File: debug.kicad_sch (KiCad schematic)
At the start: 18 parts, among them J9 USB_C_Receptacle_USB2.0, Q28 MMBT3904, Q29 MMBT3904, U16 CH340G, Y1 12MHz

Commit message: Partial layout
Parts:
- added U18: SRV05-4, Package_TO_SOT_SMD:SOT-23-6, symbol Power_Protection:SRV05-4
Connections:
- net GND: now also U18.5 (VP)
- net VBUS: now also U18.2 (VN)
- net at J9.A6 (D+), J9.B6 (D+), U16.5 (UD+): now also U18.1 (IO1)
- net at J9.A7 (D-), J9.B7 (D-), U16.6 (UD-): now also U18.3 (IO2)
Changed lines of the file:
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@@
 (kicad_sch (version 20211123) (generator eeschema)
   (paper "A4")
+  (junction (at 92.71 88.9) (diameter 0) (color 0 0 0 0)
+  )
   (junction (at 78.74 81.28) (diameter 0) (color 0 0 0 0)
   )
@@
   )
   (junction (at 124.46 72.39) (diameter 0) (color 0 0 0 0)
+  )
+  (junction (at 91.44 91.44) (diameter 0) (color 0 0 0 0)
   )
   (junction (at 41.91 113.03) (diameter 0) (color 0 0 0 0)
@@
     (stroke (width 0) (type default) (color 0 0 0 0))
   )
+  (wire (pts (xy 91.44 91.44) (xy 88.9 91.44))
+    (stroke (width 0) (type default) (color 0 0 0 0))
+  )
   (wire (pts (xy 123.19 68.58) (xy 123.19 72.39))
     (stroke (width 0) (type default) (color 0 0 0 0))
@@
     (stroke (width 0) (type default) (color 0 0 0 0))
   )
+  (wire (pts (xy 90.17 109.22) (xy 91.44 109.22))
+    (stroke (width 0) (type default) (color 0 0 0 0))
+  )
   (wire (pts (xy 31.75 113.03) (xy 41.91 113.03))
     (stroke (width 0) (type default) (color 0 0 0 0))
@@
     (stroke (width 0) (type default) (color 0 0 0 0))
   )
+  (wire (pts (xy 92.71 88.9) (xy 87.63 88.9))
+    (stroke (width 0) (type default) (color 0 0 0 0))
+  )
   (wire (pts (xy 114.3 96.52) (xy 101.6 96.52))
     (stroke (width 0) (type default) (color 0 0 0 0))
@@
     (stroke (width 0) (type default) (color 0 0 0 0))
   )
+  (wire (pts (xy 90.17 114.3) (xy 92.71 114.3))
+    (stroke (width 0) (type default) (color 0 0 0 0))
+  )
   (wire (pts (xy 134.62 101.6) (xy 146.05 101.6))
     (stroke (width 0) (type default) (color 0 0 0 0))
@@
     (stroke (width 0) (type default) (color 0 0 0 0))
   )
-  (wire (pts (xy 114.3 88.9) (xy 87.63 88.9))
+  (wire (pts (xy 114.3 88.9) (xy 92.71 88.9))
     (stroke (width 0) (type default) (color 0 0 0 0))
   )
@@
     (stroke (width 0) (type default) (color 0 0 0 0))
   )
+  (wire (pts (xy 77.47 96.52) (xy 77.47 99.06))
+    (stroke (width 0) (type default) (color 0 0 0 0))
+  )
   (wire (pts (xy 87.63 88.9) (xy 87.63 91.44))
     (stroke (width 0) (type default) (color 0 0 0 0))
@@
     (stroke (width 0) (type default) (color 0 0 0 0))
   )
-  (wire (pts (xy 114.3 91.44) (xy 88.9 91.44))
+  (wire (pts (xy 114.3 91.44) (xy 91.44 91.44))
     (stroke (width 0) (type default) (color 0 0 0 0))
   )
@@
     (stroke (width 0) (type default) (color 0 0 0 0))
   )
+  (wire (pts (xy 77.47 124.46) (xy 77.47 125.73))
+    (stroke (width 0) (type default) (color 0 0 0 0))
+  )
   (wire (pts (xy 143.51 99.06) (xy 143.51 104.14))
     (stroke (width 0) (type default) (color 0 0 0 0))
@@
   )
   (wire (pts (xy 124.46 72.39) (xy 124.46 76.2))
+    (stroke (width 0) (type default) (color 0 0 0 0))
+  )
+  (wire (pts (xy 91.44 109.22) (xy 91.44 91.44))
+    (stroke (width 0) (type default) (color 0 0 0 0))
+  )
+  (wire (pts (xy 92.71 88.9) (xy 92.71 114.3))
     (stroke (width 0) (type default) (color 0 0 0 0))
   )
@@
       (effects (font (size 1.27 1.27)) hide)
     )
-    (property "Datasheet" "https://www.usb.org/sites/default/files/documents/usb_type-c.zip" (id 3) (at 53.34 88.9 0)
+    (property "Datasheet" "https://datasheet.lcsc.com/lcsc/2103051833_Jing-Extension-of-the-Electronic-Co.-918-418K2023S40001_C167321.pdf" (id 3) (at 53.34 88.9 0)
       (effects (font (size 1.27 1.27)) hide)
     )
@@
     (pin "2")
   )
+  (symbol (lib_id "Power_Protection:SRV05-4") (at 77.47 111.76 180) (unit 1)
+    (in_bom yes) (on_board yes) (fields_autoplaced)
+    (property "Reference" "U18" (id 0) (at 77.2413 97.9002 0)
+      (effects (font (size 1.27 1.27)) (justify right))
+    )
+    (property "Value" "SRV05-4" (id 1) (at 77.2413 100.4371 0)
+      (effects (font (size 1.27 1.27)) (justify right))
+    )
+    (property "Footprint" "Package_TO_SOT_SMD:SOT-23-6" (id 2) (at 59.69 100.33 0)
+      (effects (font (size 1.27 1.27)) hide)
+    )
+    (property "Datasheet" "http://www.onsemi.com/pub/Collateral/SRV05-4-D.PDF" (id 3) (at 77.47 111.76 0)
+      (effects (font (size 1.27 1.27)) hide)
+    )
+    (property "LCSC" "C85364" (id 4) (at 77.47 111.76 0)
+      (effects (font (size 1.27 1.27)) hide)
+    )
+    (pin "1")
+    (pin "2")
+    (pin "3")
+    (pin "4")
+    (pin "5")
+    (pin "6")
+  )
   (symbol (lib_id "Device:C_Small") (at 101.6 111.76 0) (mirror x) (unit 1)
     (in_bom yes) (on_board yes) (fields_autoplaced)
@@
     (pin "2")
   )
+  (symbol (lib_id "power:VBUS") (at 77.47 96.52 0) (unit 1)
+    (in_bom yes) (on_board yes) (fields_autoplaced)
+    (property "Reference" "#PWR0305" (id 0) (at 77.47 100.33 0)
+      (effects (font (size 1.27 1.27)) hide)
+    )
+    (property "Value" "VBUS" (id 1) (at 77.47 92.9442 0))
+    (property "Footprint" "" (id 2) (at 77.47 96.52 0)
+      (effects (font (size 1.27 1.27)) hide)
+    )
+    (property "Datasheet" "" (id 3) (at 77.47 96.52 0)
+      (effects (font (size 1.27 1.27)) hide)
+    )
+    (pin "1")
+  )
   (symbol (lib_id "Device:C_Small") (at 118.11 72.39 270) (mirror x) (unit 1)
     (in_bom yes) (on_board yes)
@@
       (effects (font (size 1.27 1.27)) hide)
     )
+    (pin "1")
+  )
+  (symbol (lib_id "power:GND") (at 77.47 125.73 0) (unit 1)
+    (in_bom yes) (on_board yes) (fields_autoplaced)
+    (property "Reference" "#PWR0306" (id 0) (at 77.47 132.08 0)
+      (effects (font (size 1.27 1.27)) hide)
+    )
+    (property "Value" "GND" (id 1) (at 77.47 130.1734 0))
+    (property "Footprint" "" (id 2) (at 77.47 125.73 0)
+      (effects (font (size 1.27 1.27)) hide)
+    )
+    (property "Datasheet" "" (id 3) (at 77.47 125.73 0)
+      (effects (font (size 1.27 1.27)) hide)
+    )

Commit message: Fix footprint origins for JLC assembly
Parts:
- U16: value CH340G -> CH340C; LCSC C14267 -> C84681
- Y1: value 12MHz -> 12MHz (DNP); now left out of the parts list
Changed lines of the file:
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@@
       (effects (font (size 1.27 1.27)) (justify left))
     )
-    (property "Value" "CH340G" (id 1) (at 126.4794 108.7073 0)
+    (property "Value" "CH340C" (id 1) (at 126.4794 108.7073 0)
       (effects (font (size 1.27 1.27)) (justify left))
     )
@@
       (effects (font (size 1.27 1.27)) hide)
     )
-    (property "LCSC" "C14267" (id 4) (at 124.46 91.44 0)
+    (property "LCSC" "C84681" (id 4) (at 124.46 91.44 0)
       (effects (font (size 1.27 1.27)) hide)
     )
@@
   )
   (symbol (lib_id "Device:Crystal_GND24_Small") (at 105.41 107.95 0) (unit 1)
-    (in_bom yes) (on_board yes)
+    (in_bom no) (on_board yes)
     (property "Reference" "Y1" (id 0) (at 113.03 104.14 0))
-    (property "Value" "12MHz" (id 1) (at 113.03 106.68 0))
+    (property "Value" "12MHz (DNP)" (id 1) (at 113.03 106.68 0))
     (property "Footprint" "Crystal:Crystal_SMD_3225-4Pin_3.2x2.5mm" (id 2) (at 105.41 107.95 0)
       (effects (font (size 1.27 1.27)) hide)

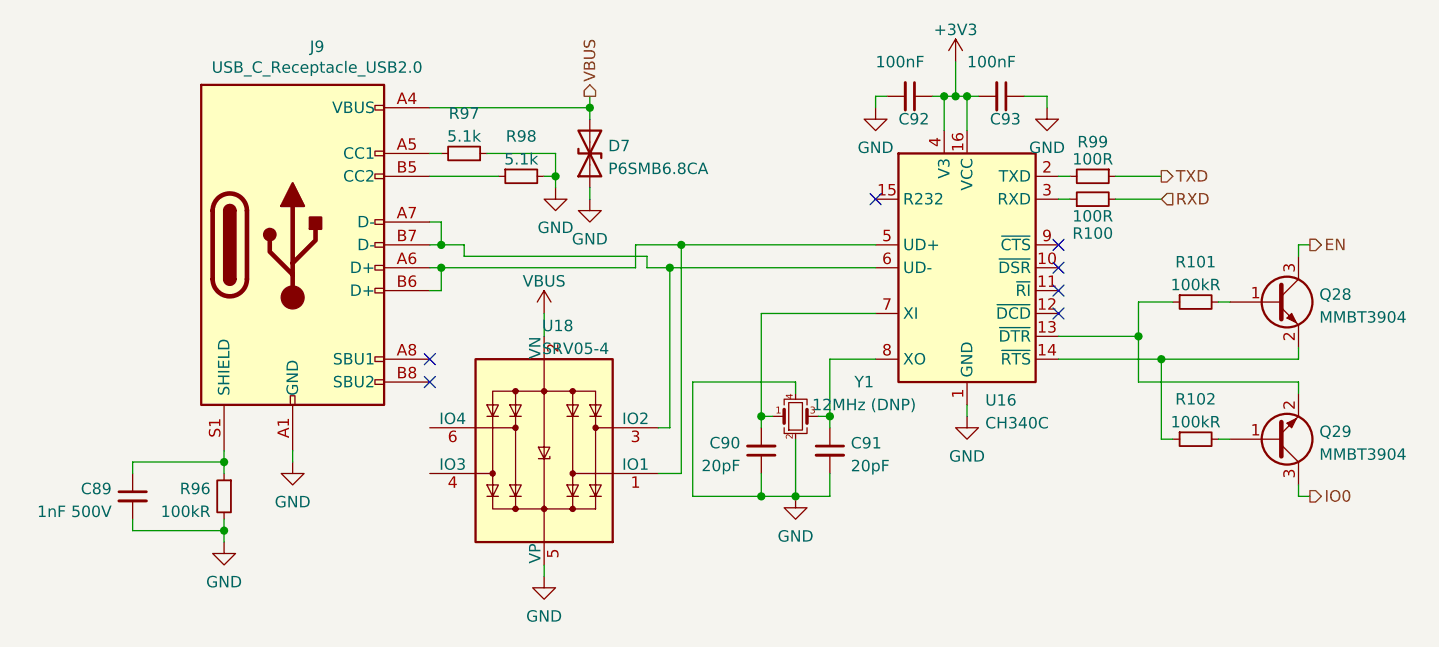
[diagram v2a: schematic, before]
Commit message: Fix reversed debug USB TVS
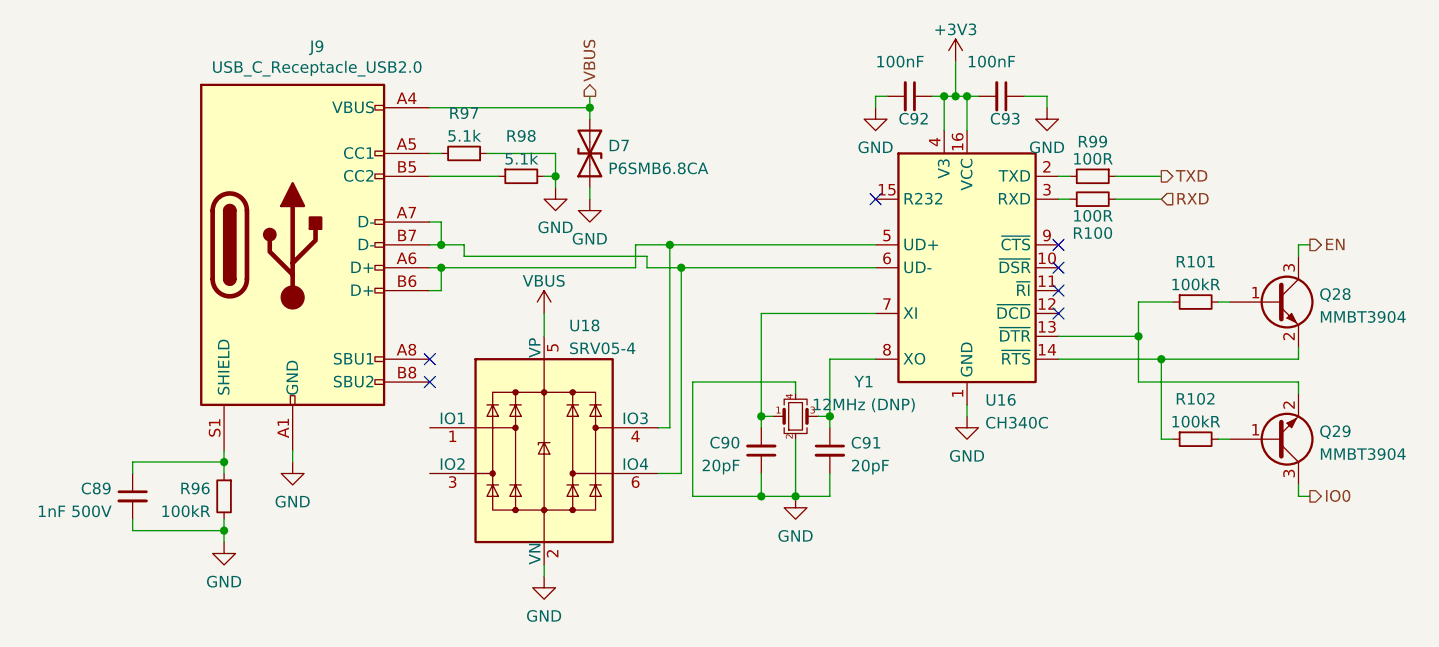
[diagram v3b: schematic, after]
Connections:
- net GND: now also U18.2 (VN); no longer U18.5 (VP)
- net VBUS: now also U18.5 (VP); no longer U18.2 (VN)
- net at J9.A6 (D+), J9.B6 (D+), U16.5 (UD+): now also U18.4 (IO3); no longer U18.1 (IO1)
- net at J9.A7 (D-), J9.B7 (D-), U16.6 (UD-): now also U18.6 (IO4); no longer U18.3 (IO2)
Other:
- moved on the sheet: U18
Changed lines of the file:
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@@
 (kicad_sch (version 20211123) (generator eeschema)
   (paper "A4")
-  (junction (at 92.71 88.9) (diameter 0) (color 0 0 0 0)
-  )
   (junction (at 78.74 81.28) (diameter 0) (color 0 0 0 0)
   )
@@
   (junction (at 105.41 116.84) (diameter 0) (color 0 0 0 0)
   )
+  (junction (at 92.71 91.44) (diameter 0) (color 0 0 0 0)
+  )
   (junction (at 101.6 107.95) (diameter 0) (color 0 0 0 0)
   )
@@
   (junction (at 124.46 72.39) (diameter 0) (color 0 0 0 0)
   )
-  (junction (at 91.44 91.44) (diameter 0) (color 0 0 0 0)
-  )
   (junction (at 41.91 113.03) (diameter 0) (color 0 0 0 0)
   )
@@
   )
   (junction (at 143.51 99.06) (diameter 0) (color 0 0 0 0)
+  )
+  (junction (at 91.44 88.9) (diameter 0) (color 0 0 0 0)
   )
   (no_connect (at 64.77 104.14))
@@
     (stroke (width 0) (type default) (color 0 0 0 0))
   )
-  (wire (pts (xy 91.44 91.44) (xy 88.9 91.44))
+  (wire (pts (xy 88.9 91.44) (xy 92.71 91.44))
     (stroke (width 0) (type default) (color 0 0 0 0))
   )
@@
     (stroke (width 0) (type default) (color 0 0 0 0))
   )
-  (wire (pts (xy 92.71 88.9) (xy 87.63 88.9))
+  (wire (pts (xy 87.63 88.9) (xy 91.44 88.9))
     (stroke (width 0) (type default) (color 0 0 0 0))
   )
@@
     (stroke (width 0) (type default) (color 0 0 0 0))
   )
+  (wire (pts (xy 91.44 88.9) (xy 91.44 109.22))
+    (stroke (width 0) (type default) (color 0 0 0 0))
+  )
   (wire (pts (xy 130.81 72.39) (xy 133.35 72.39))
     (stroke (width 0) (type default) (color 0 0 0 0))
@@
     (stroke (width 0) (type default) (color 0 0 0 0))
   )
+  (wire (pts (xy 92.71 91.44) (xy 114.3 91.44))
+    (stroke (width 0) (type default) (color 0 0 0 0))
+  )
   (wire (pts (xy 64.77 78.74) (xy 66.04 78.74))
     (stroke (width 0) (type default) (color 0 0 0 0))
@@
     (stroke (width 0) (type default) (color 0 0 0 0))
   )
-  (wire (pts (xy 114.3 88.9) (xy 92.71 88.9))
-    (stroke (width 0) (type default) (color 0 0 0 0))
-  )
   (wire (pts (xy 143.51 95.25) (xy 147.32 95.25))
     (stroke (width 0) (type default) (color 0 0 0 0))
   )
+  (wire (pts (xy 92.71 91.44) (xy 92.71 114.3))
+    (stroke (width 0) (type default) (color 0 0 0 0))
+  )
   (wire (pts (xy 105.41 104.14) (xy 93.98 104.14))
     (stroke (width 0) (type default) (color 0 0 0 0))
@@
     (stroke (width 0) (type default) (color 0 0 0 0))
   )
-  (wire (pts (xy 114.3 91.44) (xy 91.44 91.44))
-    (stroke (width 0) (type default) (color 0 0 0 0))
-  )
   (wire (pts (xy 68.58 90.17) (xy 68.58 88.9))
     (stroke (width 0) (type default) (color 0 0 0 0))
@@
     (stroke (width 0) (type default) (color 0 0 0 0))
   )
+  (wire (pts (xy 91.44 88.9) (xy 114.3 88.9))
+    (stroke (width 0) (type default) (color 0 0 0 0))
+  )
   (wire (pts (xy 134.62 81.28) (xy 135.89 81.28))
     (stroke (width 0) (type default) (color 0 0 0 0))
@@
   )
   (wire (pts (xy 124.46 72.39) (xy 124.46 76.2))
-    (stroke (width 0) (type default) (color 0 0 0 0))
-  )
-  (wire (pts (xy 91.44 109.22) (xy 91.44 91.44))
-    (stroke (width 0) (type default) (color 0 0 0 0))
-  )
-  (wire (pts (xy 92.71 88.9) (xy 92.71 114.3))
     (stroke (width 0) (type default) (color 0 0 0 0))
   )
@@
     (pin "2")
   )
-  (symbol (lib_id "Power_Protection:SRV05-4") (at 77.47 111.76 180) (unit 1)
-    (in_bom yes) (on_board yes) (fields_autoplaced)
-    (property "Reference" "U18" (id 0) (at 77.2413 97.9002 0)
-      (effects (font (size 1.27 1.27)) (justify right))
-    )
-    (property "Value" "SRV05-4" (id 1) (at 77.2413 100.4371 0)
-      (effects (font (size 1.27 1.27)) (justify right))
-    )
-    (property "Footprint" "Package_TO_SOT_SMD:SOT-23-6" (id 2) (at 59.69 100.33 0)
-      (effects (font (size 1.27 1.27)) hide)
-    )
+  (symbol (lib_id "Power_Protection:SRV05-4") (at 77.47 111.76 0) (unit 1)
+    (in_bom yes) (on_board yes) (fields_autoplaced)
+    (property "Reference" "U18" (id 0) (at 80.2387 97.9002 0)
+      (effects (font (size 1.27 1.27)) (justify left))
+    )
+    (property "Value" "SRV05-4" (id 1) (at 80.2387 100.4371 0)
+      (effects (font (size 1.27 1.27)) (justify left))
+    )
+    (property "Footprint" "Package_TO_SOT_SMD:SOT-23-6" (id 2) (at 95.25 123.19 0)
+      (effects (font (size 1.27 1.27)) hide)
+    )

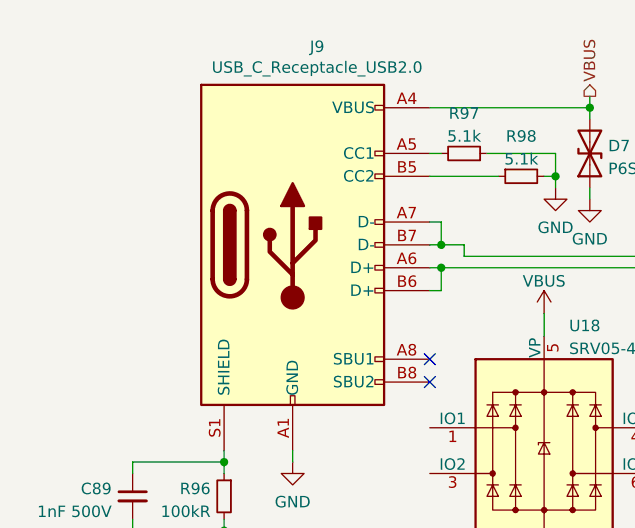
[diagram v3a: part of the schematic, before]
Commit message: Rev 1.0 bugfixes
Changes:
 - Replace DCOK-driven DC passthrough switch with ideal diode
 - Reduce INA219 series filter resistance to 1 ohm
 - Simplify debug USB power gating
 - Fix incorrect USB CC pullups
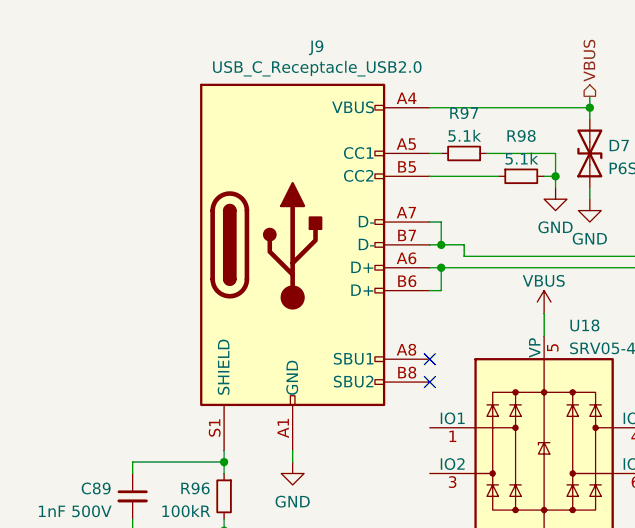
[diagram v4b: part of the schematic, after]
